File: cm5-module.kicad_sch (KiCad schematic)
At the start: 0 parts

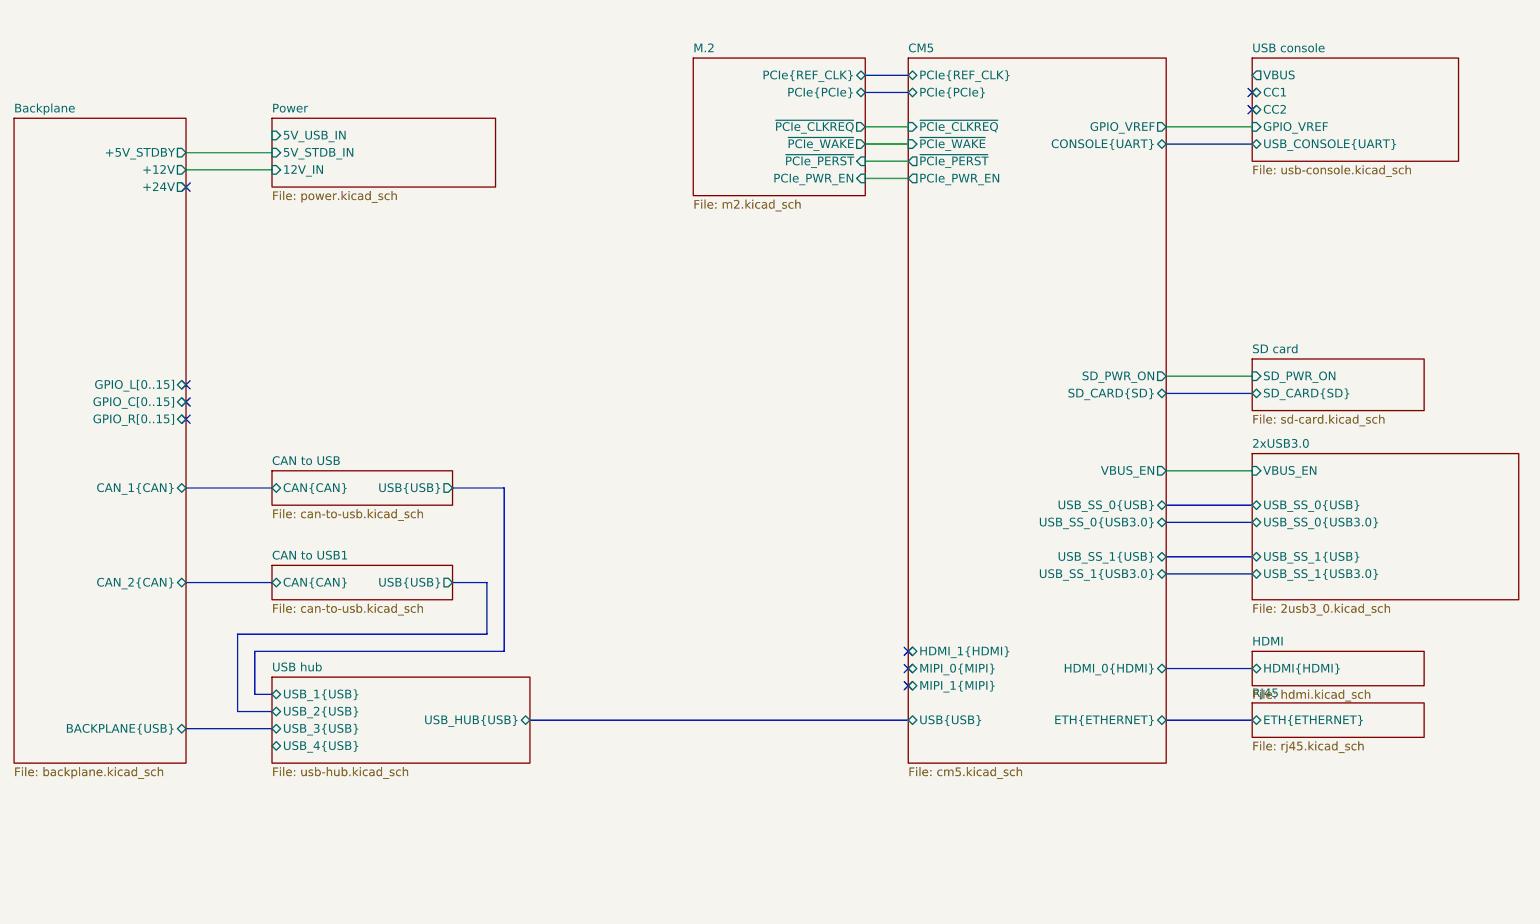
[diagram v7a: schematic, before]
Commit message: [#1] WIP: Refactor schematic
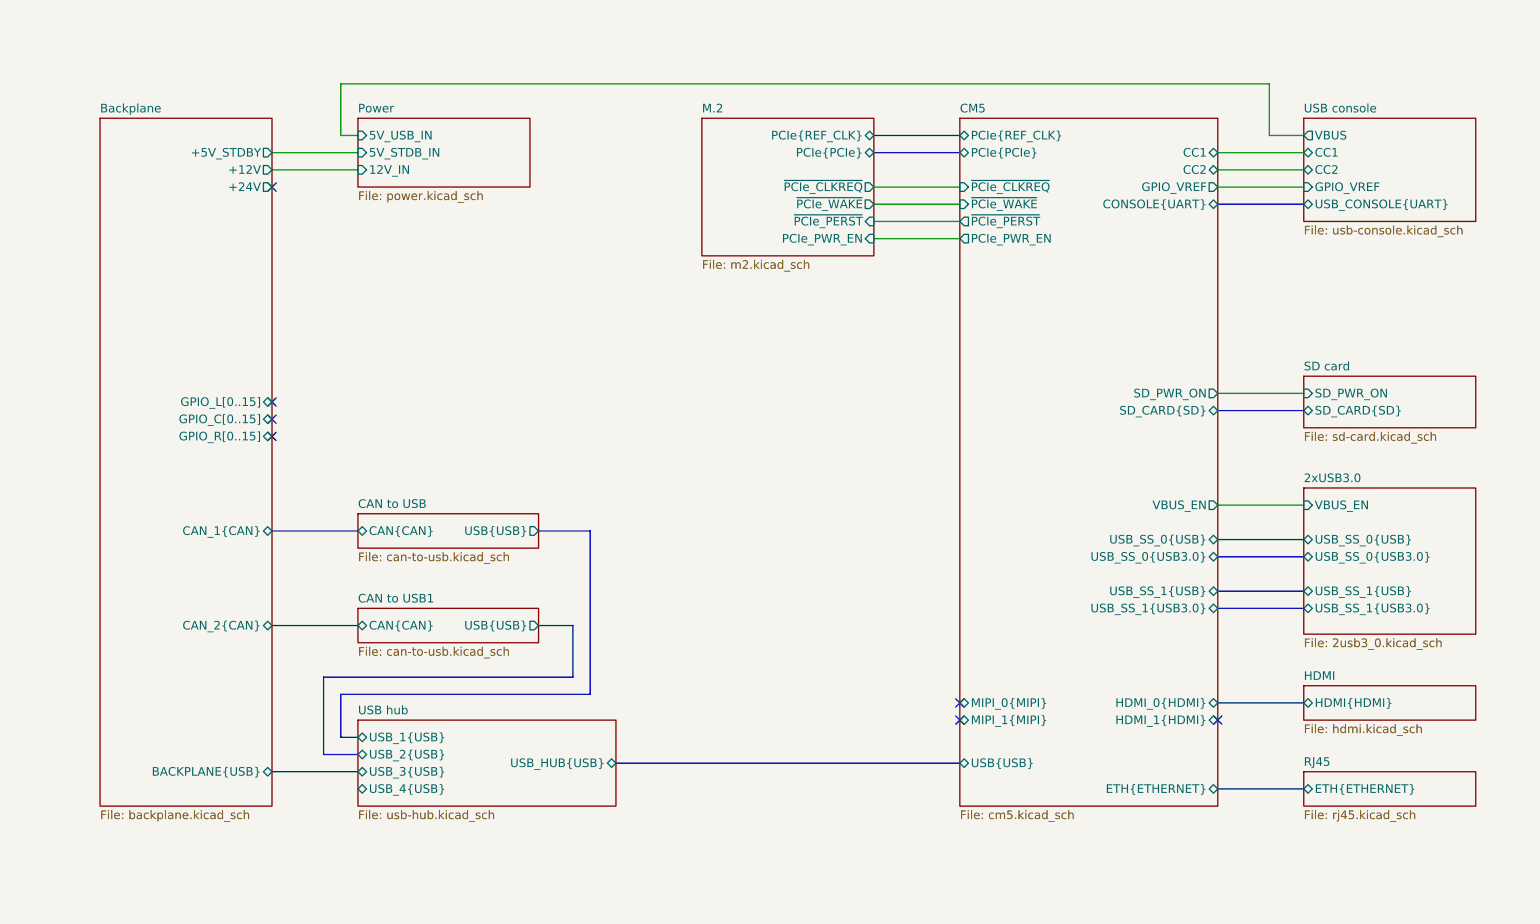
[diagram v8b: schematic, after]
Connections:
- no-connect marks 9 -> 7
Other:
- sheet CM5 ports: added CC1, CC2; removed none
